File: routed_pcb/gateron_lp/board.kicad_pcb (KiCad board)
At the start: 2 copper layers, 100 x 100 mm, 28 parts

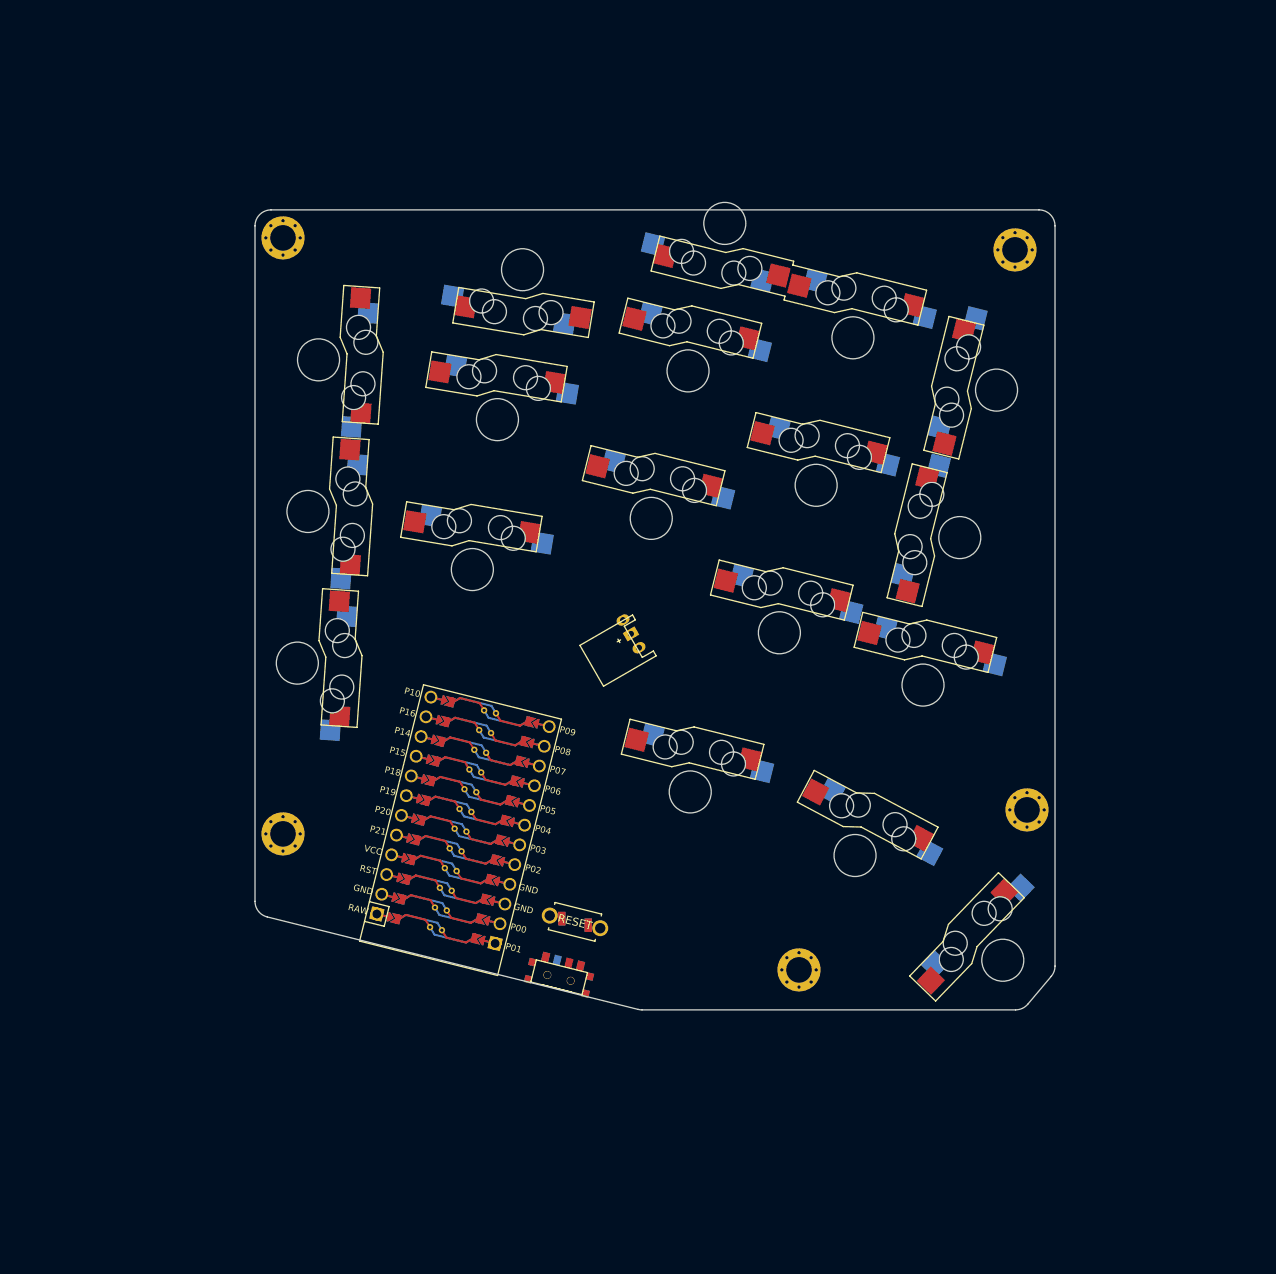
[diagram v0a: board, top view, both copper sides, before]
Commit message: cleaned up config file, routed gateron pcb
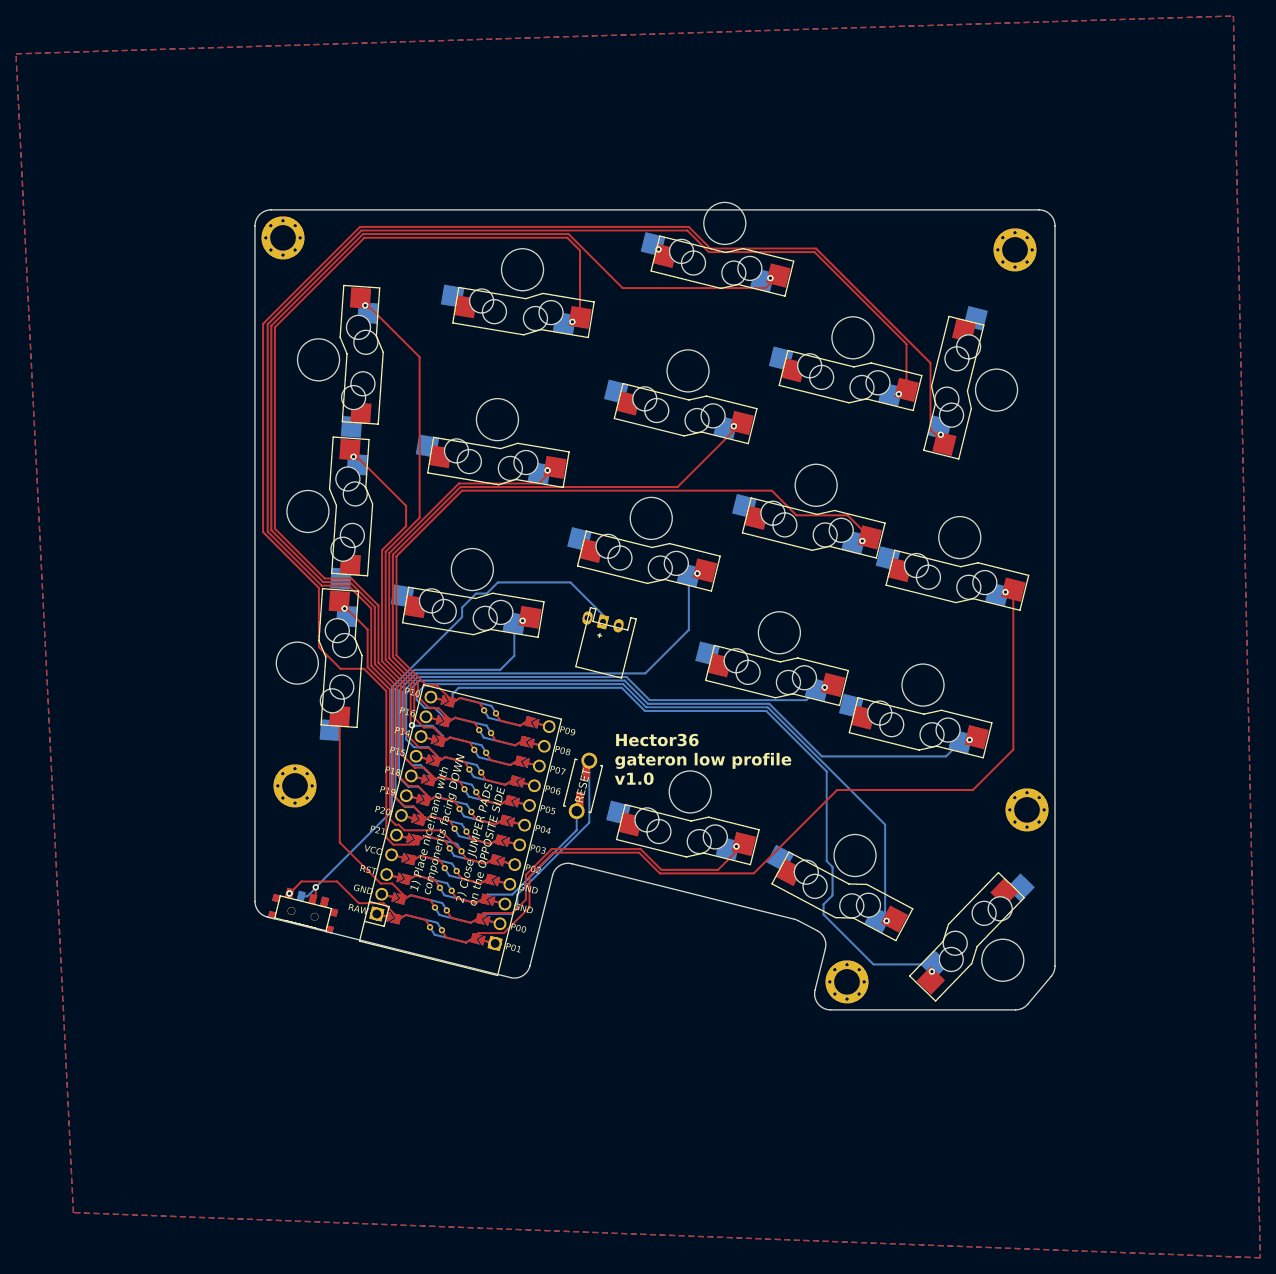
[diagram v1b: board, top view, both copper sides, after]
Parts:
- moved T1 33.0 mm to (89.5, 137.8)
- moved B1 17.0 mm to (124.5, 121.8), turned to -104 degrees
- moved B2 17.0 mm to (124.5, 121.8), turned to 76 degrees
- moved HOLE4 6.18 mm to (157.5, 146.3)
- moved HOLE5 6.18 mm to (88.5, 121.8)
- moved JST1 3.81 mm to (127.0, 101.3), turned to -14 degrees
- turned SW1 to 86 degrees
- turned SW2 to 86 degrees
- turned SW3 to 86 degrees
- turned SW6 to -9.5 degrees
- turned SW18 to -134 degrees
- turned SW9 to -14 degrees
- turned SW15 to -104 degrees
- turned SW14 to -14 degrees
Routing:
- net matrix_inner_top: track 0.00 -> 183.6 mm, vias 0 -> 1
- net matrix_index_top: track 0.00 -> 169.0 mm, vias 0 -> 1
- net matrix_middle_top: track 0.00 -> 142.1 mm, vias 0 -> 1
- net matrix_ring_top: track 0.00 -> 119.4 mm, vias 0 -> 1
- net matrix_inner_home: track 0.00 -> 101.7 mm, vias 0 -> 1
- net thumb_reachy: track 0.00 -> 87.6 mm, vias 0 -> 1
- net matrix_index_home: track 0.00 -> 86.9 mm, vias 0 -> 1
- net matrix_inner_bottom: track 0.00 -> 85.8 mm, vias 0 -> 1
- net thumb_tucky: track 0.00 -> 84.5 mm, vias 0 -> 1
- net matrix_middle_home: track 0.00 -> 75.2 mm, vias 0 -> 1
- net Bplus: track 0.00 -> 68.0 mm, vias 0 -> 1
- net matrix_index_bottom: track 0.00 -> 67.7 mm, vias 0 -> 1
- net matrix_pinky_top: track 0.00 -> 65.2 mm, vias 0 -> 2
- net matrix_middle_bottom: track 0.00 -> 62.3 mm, vias 0 -> 1
- net GND: track 0.00 -> 54.6 mm, vias 0 -> 1
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- added copper zone on B.Cu, net GND
- added copper zone on F.Cu, net GND
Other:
- outline, holes or cut-outs redrawn
- net class Default removed
- board text added: "1) Place nice!nano with components facing DOWN"
- board text added: "2) Close JUMPER PADS on the OPPOSITE SIDE"
- board text added: "Hector36 gateron low profile v1.0"
